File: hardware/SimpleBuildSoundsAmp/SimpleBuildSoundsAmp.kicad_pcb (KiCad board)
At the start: 2 copper layers, 68.5 x 47.1 mm, 34 parts, among them J1 Power and GoBtn, J14 Volume, J15 Left Speaker, J2 RJ45, J3 Other Button, J4 Power, J5 FX_Sound, Q1 AOD417, U4 MAX9744

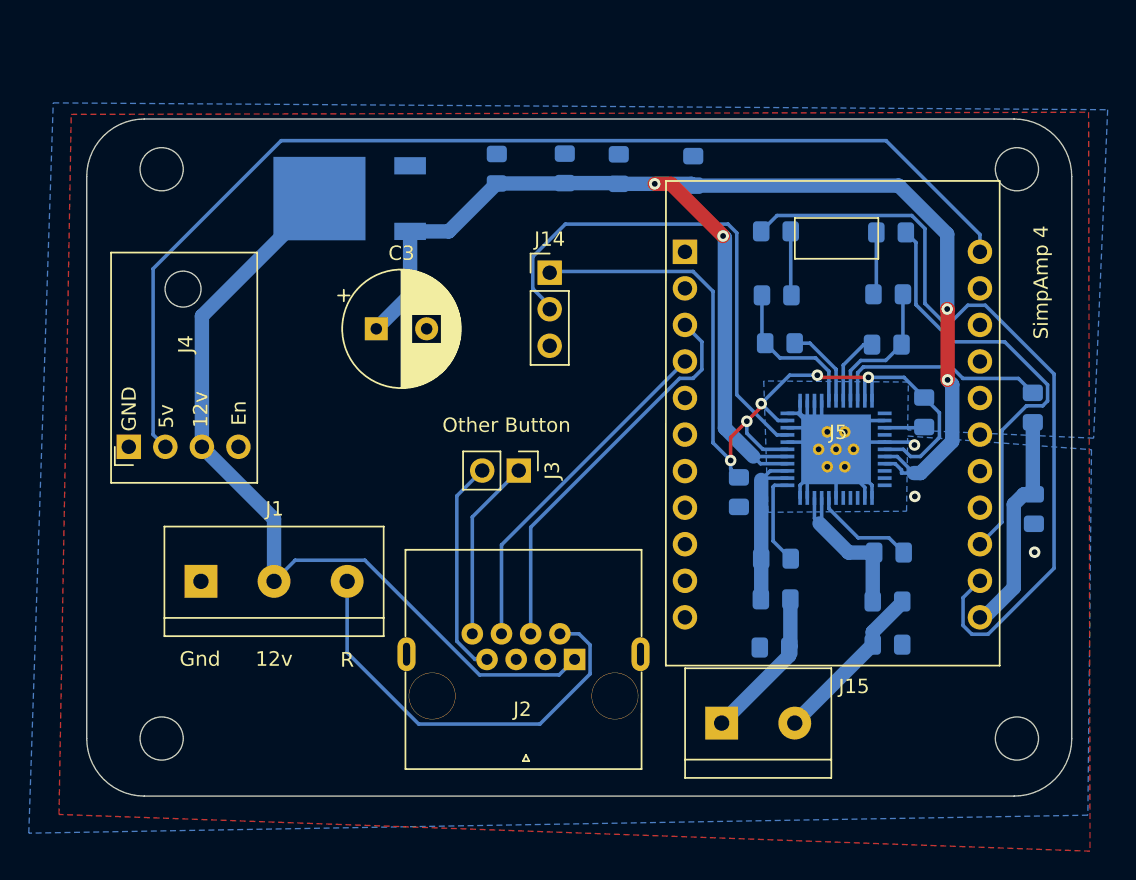
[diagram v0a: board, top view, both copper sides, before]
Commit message: Added 3v regulator and minor adjustments
Added 3v regulator. Moved power label way from screw terminal. Added label for volume. Added label for Speaker wires. Added USB text on usb side of sound board.
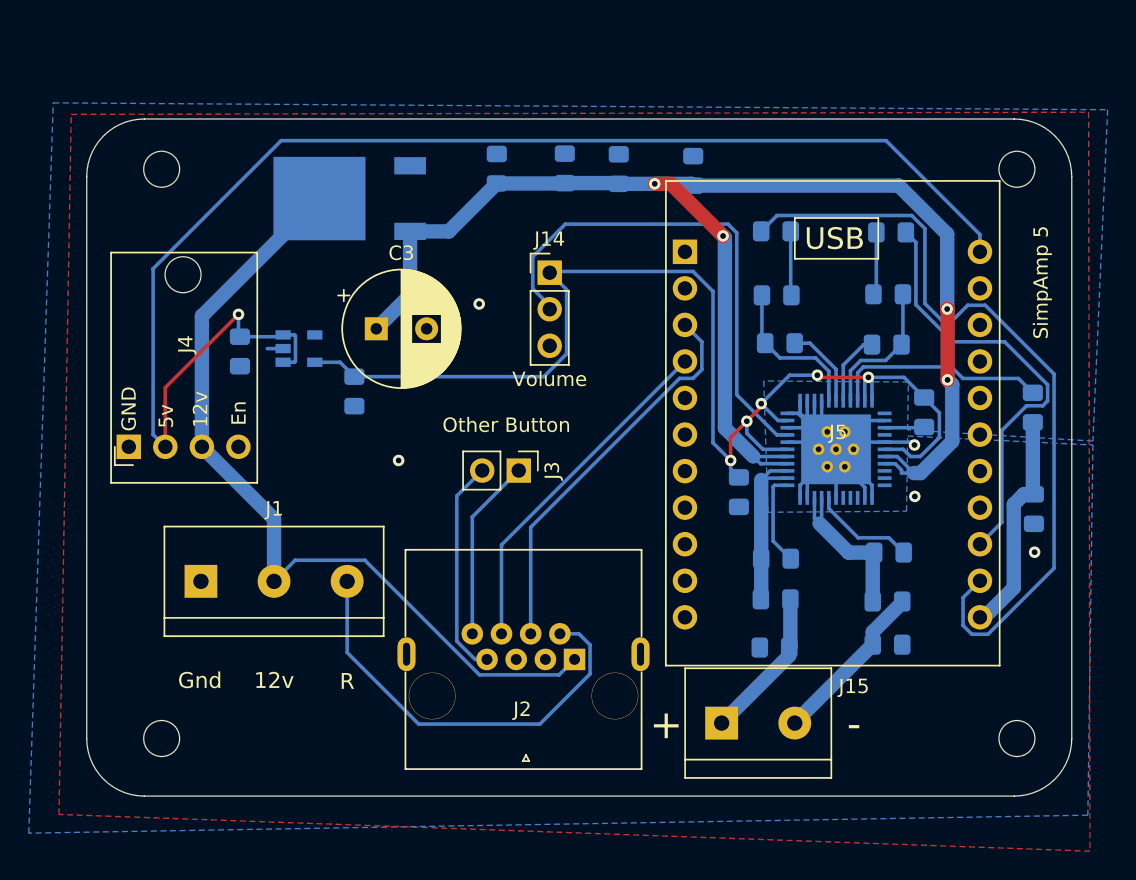
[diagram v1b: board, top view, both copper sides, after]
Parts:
- added C11: 1µF, Capacitor_SMD:C_0805_2012Metric_Pad1.15x1.40mm_HandSolder, B.Cu at (144.1, 64.2)
- added C14: 1µF, Capacitor_SMD:C_0805_2012Metric_Pad1.15x1.40mm_HandSolder, B.Cu at (152.1, 67.0)
- added U1: AP2112K-3.3, Package_TO_SOT_SMD:SOT-23-5, B.Cu at (148.2, 64.0)
- REF (x4): value MountingHole_3mm -> MountingHole_2.5mm; footprint MountingHole:MountingHole_3mm -> MountingHole:MountingHole_2.5mm
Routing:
- net +3V3: track 61.1 -> 85.8 mm
- net +5V: track 77.8 -> 97.2 mm, vias 0 -> 1
- net GND: track 56.9 -> 58.0 mm, vias 3 -> 5
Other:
- board text added: "+"
- board text added: "-"
- board text added: "SimpAmp 5"
- board text added: "USB"
- board text removed: "SimpAmp 4"

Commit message: Broke out Terminals to allow for Simple Caddy
Updates that will help with making a Caddy for the simple Go Button cars. Spilt the power/relay terminal into two terminals and moved them to the other side of the board. This will allow for the removal of the WAGO connectors when wiring.
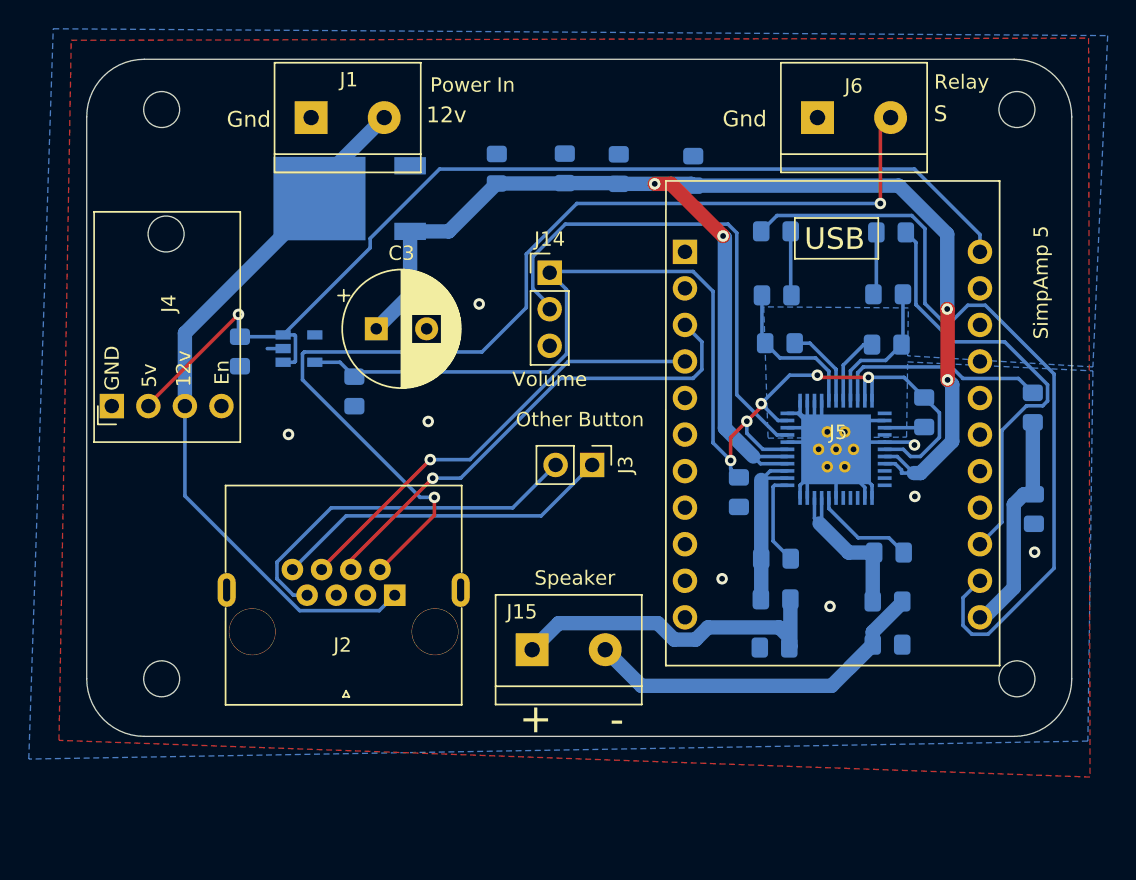
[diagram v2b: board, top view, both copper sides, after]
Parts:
- added J6: Relay, Useful Modifications:TerminalBlock_bornier-2_P5.08mm, F.Cu at (184.3, 48.0)
- J1: value Power and GoBtn -> Power In
- J15: value Left Speaker -> Speaker
- moved J1 33.1 mm to (149.1, 48.0)
- moved J15 14.1 mm to (164.4, 85.0)
- moved J2 13.3 mm to (151.1, 84.8)
- moved J3 5.11 mm to (168.6, 72.1)
- moved REF 4.15 mm to (138.7, 87.0)
- moved REF 4.15 mm to (198.1, 87.0)
- moved REF 4.15 mm to (138.7, 47.4)
- moved REF 4.15 mm to (198.1, 47.4)
- moved J4 3.07 mm to (135.2, 68.0)
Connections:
- J2 pad 2: Net-(J1-Pad3) -> Net-(J2-Pad2)
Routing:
- net Net-(J2-Pad2): track 0.00 -> 73.9 mm, vias 0 -> 2
- net Net-(J1-Pad3): track 29.8 -> 0.00 mm
- net +5V: track 97.2 -> 73.8 mm
- net Net-(C13-Pad1): track 11.5 -> 26.9 mm
- net Net-(C12-Pad2): track 10.6 -> 23.8 mm
- net Net-(J2-Pad8): track 12.7 -> 23.8 mm
- net Net-(J2-Pad7): track 15.2 -> 25.9 mm
- net Net-(J2-Pad6): track 24.2 -> 31.3 mm, vias 0 -> 1
- net +12V: track 57.3 -> 50.4 mm
- net Net-(J2-Pad4): track 27.4 -> 34.1 mm, vias 0 -> 1
- net GND: vias 5 -> 8
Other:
- board text added: "S"
- board text removed: "R"

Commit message: isolating 12v and amp from microcontroller
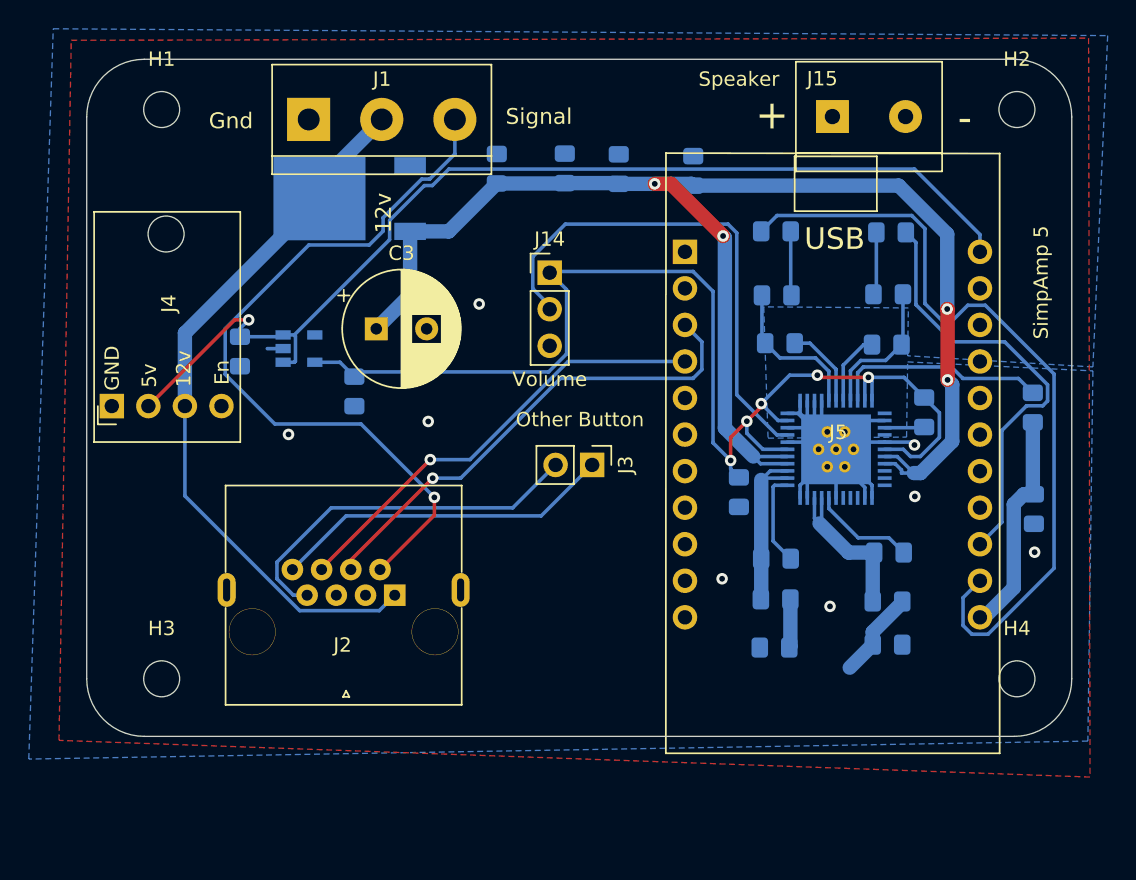
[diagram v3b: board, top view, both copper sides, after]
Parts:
- removed J6: Relay, Useful Modifications:TerminalBlock_bornier-2_P5.08mm
- removed REF (x4): MountingHole_2.5mm, MountingHole:MountingHole_2.5mm
- added H1: MountingHole, MountingHole:MountingHole_2.5mm, F.Cu at (138.7, 47.4)
- added H2: MountingHole, MountingHole:MountingHole_2.5mm, F.Cu at (198.1, 47.4)
- added H3: MountingHole, MountingHole:MountingHole_2.5mm, F.Cu at (138.7, 87.0)
- added H4: MountingHole, MountingHole:MountingHole_2.5mm, F.Cu at (198.1, 87.0)
- J1: value Power In -> Power/Relay; footprint Useful Modifications:TerminalBlock_bornier-2_P5.08mm -> TerminalBlock:TerminalBlock_bornier-3_P5.08mm
- J5: footprint Useful Modifications:FXSound_2x11_P2.54mm_Short -> Useful Modifications:FXSound_2x11_P2.54mm
- moved J15 42.5 mm to (185.3, 47.9)
- moved J1 0.21 mm to (148.9, 48.1)
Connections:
- J2 pad 2: Net-(J2-Pad2) -> Net-(J1-Pad3)
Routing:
- net Net-(J2-Pad2): track 73.9 -> 0.00 mm, vias 2 -> 0
- net Net-(J1-Pad3): track 0.00 -> 51.8 mm, vias 0 -> 1
- net Net-(C13-Pad1): track 26.9 -> 6.11 mm
- net Net-(C12-Pad2): track 23.8 -> 3.38 mm
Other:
- board text added: "Signal"
- board text removed: "S"

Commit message: Connected speaker traces
Connected the speaker traces and updated some items on the silk screen.
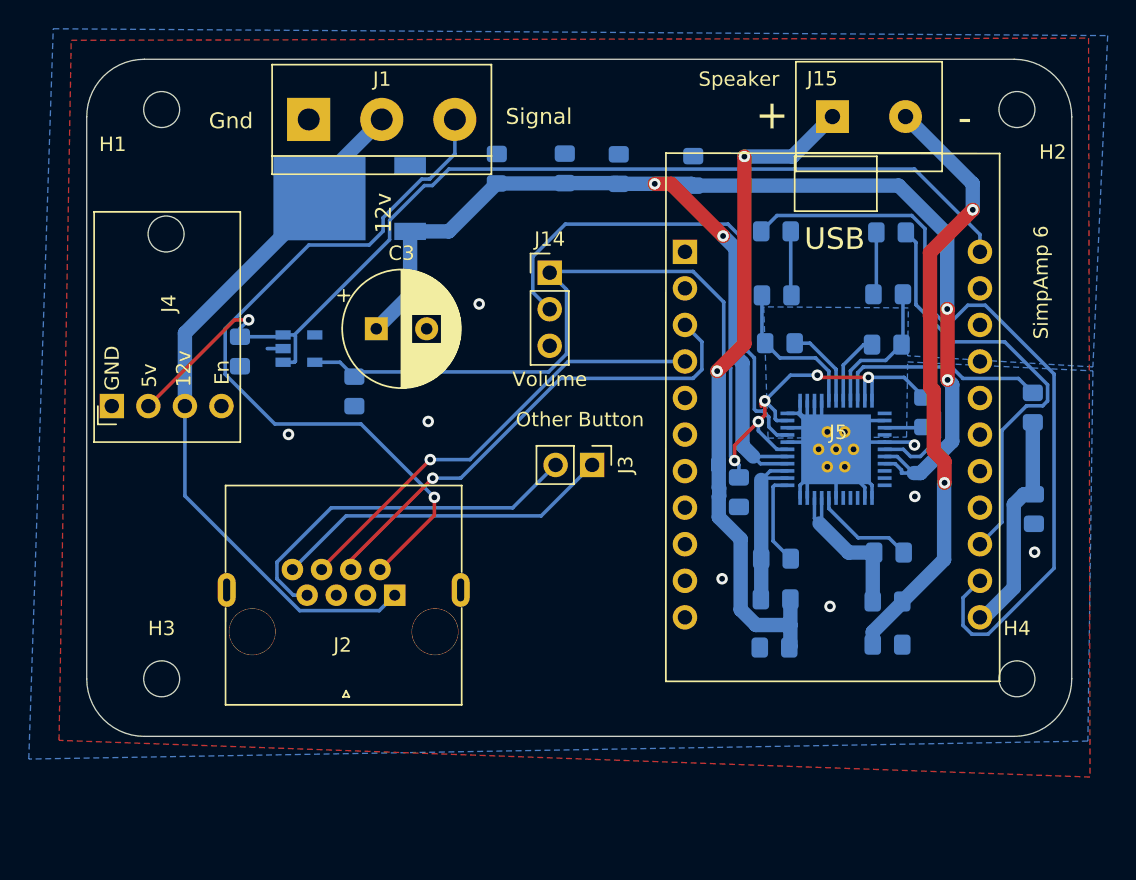
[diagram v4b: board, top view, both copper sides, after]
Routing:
- net Net-(C12-Pad2): track 3.38 -> 48.0 mm, vias 0 -> 2
- net Net-(C13-Pad1): track 6.11 -> 42.4 mm, vias 0 -> 2
- net +3V3: track 85.8 -> 85.2 mm
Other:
- board text added: "SimpAmp 6"
- board text removed: "SimpAmp 5"

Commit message: Added JST connector for Volume
JST connector is 2.54 pitch. Added ground line on resistor R9.
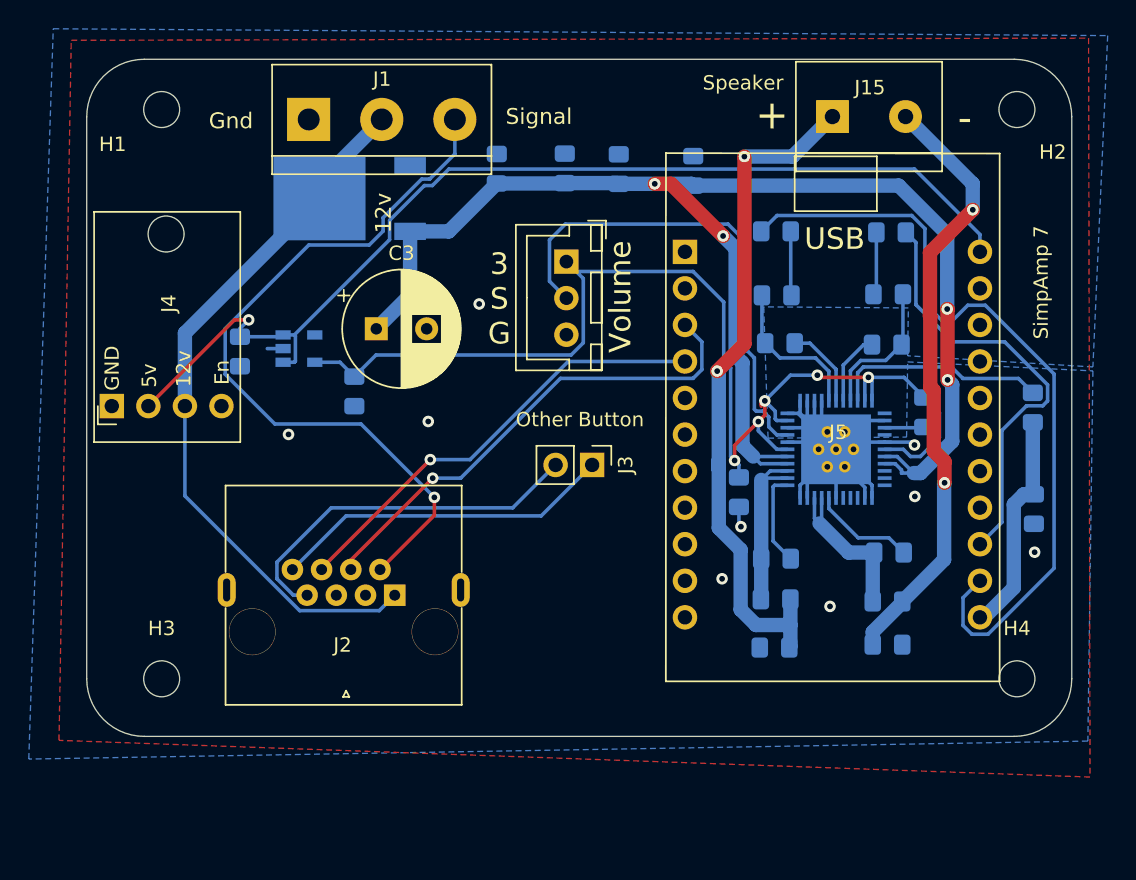
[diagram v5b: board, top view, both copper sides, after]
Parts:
- removed J14: Volume, Connector_PinHeader_2.54mm:PinHeader_1x03_P2.54mm_Vertical
- added Volume: Volume, Useful Modifications:JST_XH_B3B-XH-A_1x03_P2.54mm_Vertical, F.Cu at (166.8, 58.0)
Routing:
- net GND: track 58.0 -> 59.4 mm, vias 8 -> 9
- net Net-(J14-Pad2): track 35.7 -> 34.5 mm
- net +3V3: track 85.2 -> 86.2 mm
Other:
- board text added: "3 S G"
- board text added: "SimpAmp 7"
- board text removed: "SimpAmp 6"

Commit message: Added Sound Pin Breakout
KiCad 6
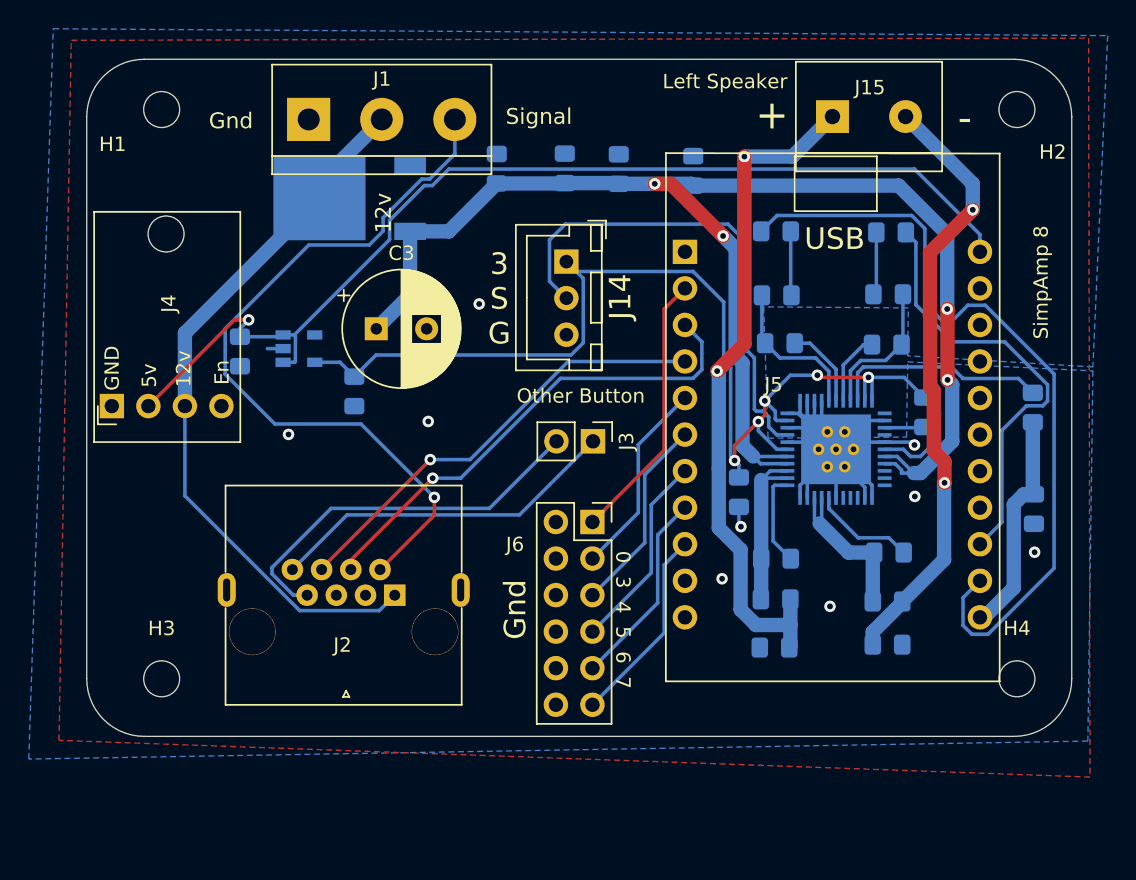
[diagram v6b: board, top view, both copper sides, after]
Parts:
- added J6: Additional Sounds, Connector_PinSocket_2.54mm:PinSocket_2x06_P2.54mm_Vertical, F.Cu at (168.6, 76.1)
- J15: value Speaker -> Left Speaker
- moved J3 1.64 mm to (168.7, 70.5)
- renumbered Volume to J14
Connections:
- net +3V3 renamed +3.3V
- J4 pad 4: Net-(J4-Pad4) -> unconnected-(J4-Pad4)
- J5 pad 1: Net-(J5-Pad1) -> unconnected-(J5-Pad1)
- J5 pad 10: Net-(J5-Pad10) -> unconnected-(J5-Pad10)
- J5 pad 11: Net-(J5-Pad11) -> Sound4
- J5 pad 12: Net-(J5-Pad12) -> unconnected-(J5-Pad12)
- J5 pad 13: Net-(J5-Pad13) -> Sound5
- J5 pad 14: Net-(J5-Pad14) -> unconnected-(J5-Pad14)
- J5 pad 15: Net-(J5-Pad15) -> Sound6
- J5 pad 16: Net-(J5-Pad16) -> unconnected-(J5-Pad16)
- J5 pad 17: Net-(J5-Pad17) -> Sound7
- J5 pad 19: Net-(J5-Pad19) -> unconnected-(J5-Pad19)
- J5 pad 21: Net-(J5-Pad21) -> unconnected-(J5-Pad21)
- J5 pad 3: Net-(J5-Pad3) -> Sound0
- J5 pad 6: Net-(J5-Pad6) -> unconnected-(J5-Pad6)
- J5 pad 8: Net-(J5-Pad8) -> unconnected-(J5-Pad8)
- J5 pad 9: Net-(J5-Pad9) -> Sound3
- U1 pad 4: Net-(U1-Pad4) -> unconnected-(U1-Pad4)
- U4 pad 23: Net-(U4-Pad23) -> unconnected-(U4-Pad23)
- U4 pad 26: Net-(U4-Pad26) -> unconnected-(U4-Pad26)
- U4 pad 31: Net-(U4-Pad31) -> unconnected-(U4-Pad31)
- U4 pad 32: Net-(U4-Pad32) -> unconnected-(U4-Pad32)
- U4 pad 33: Net-(U4-Pad33) -> unconnected-(U4-Pad33)
- U4 pad 36: Net-(U4-Pad36) -> unconnected-(U4-Pad36)
- U4 pad 37: Net-(U4-Pad37) -> unconnected-(U4-Pad37)
- U4 pad 38: Net-(U4-Pad38) -> unconnected-(U4-Pad38)
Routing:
- net Sound0: track 0.00 -> 18.9 mm
- net Sound7: track 0.00 -> 13.8 mm
- net Sound3: track 0.00 -> 13.8 mm
- net Sound6: track 0.00 -> 13.8 mm
- net Sound4: track 0.00 -> 13.8 mm
- net Sound5: track 0.00 -> 13.8 mm
- net Net-(J2-Pad7): track 25.9 -> 26.9 mm
- net +3.3V: track 86.2 -> 85.2 mm
- net Net-(J2-Pad8): track 23.8 -> 24.6 mm
- net Net-(C12-Pad2): track 48.0 -> 47.5 mm
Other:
- net class Default removed
- board text added: "0 3 4 5 6 7"
- board text added: "SimpAmp 8"
- board text removed: "SimpAmp 7"
